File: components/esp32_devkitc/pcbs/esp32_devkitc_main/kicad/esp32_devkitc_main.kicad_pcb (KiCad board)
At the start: 2 copper layers, 65 x 56 mm, 10 parts, among them P1 Conn_02x20_Odd_Even

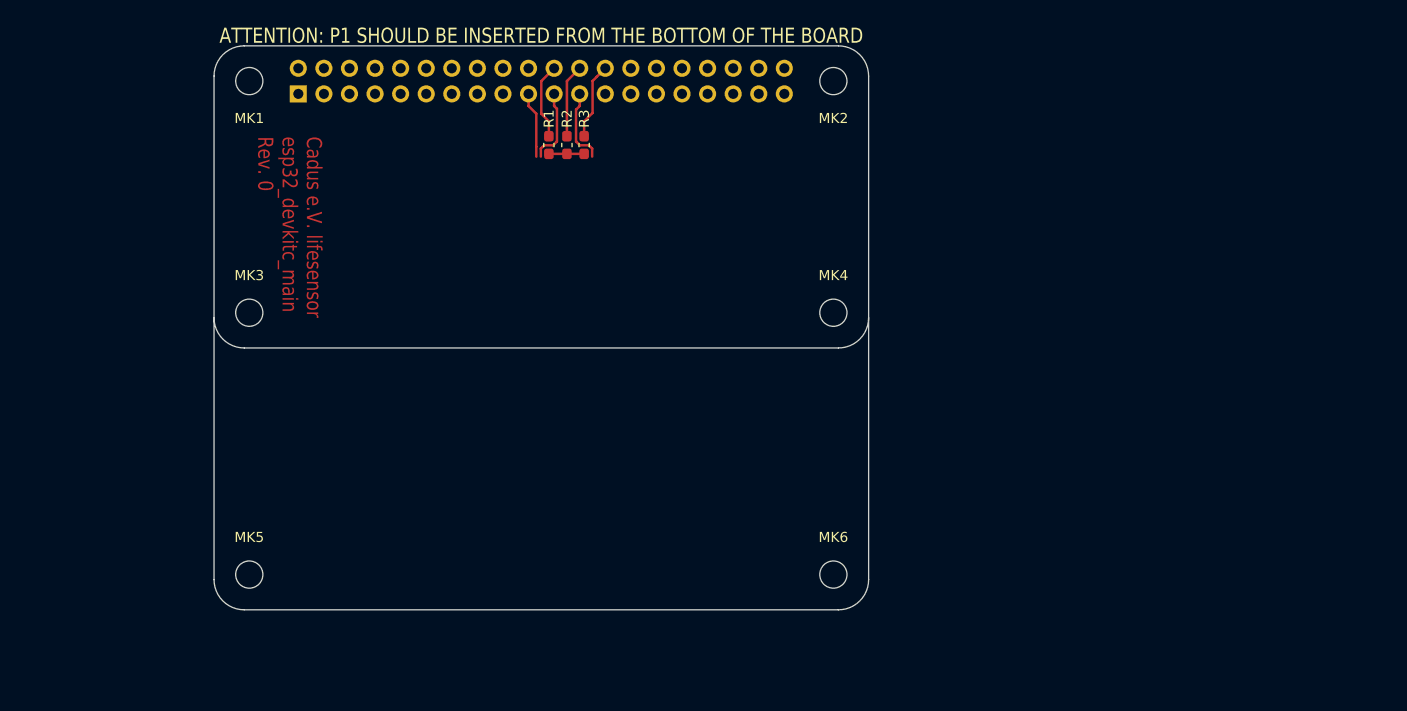
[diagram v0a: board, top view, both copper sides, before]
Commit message: add devkitc to board
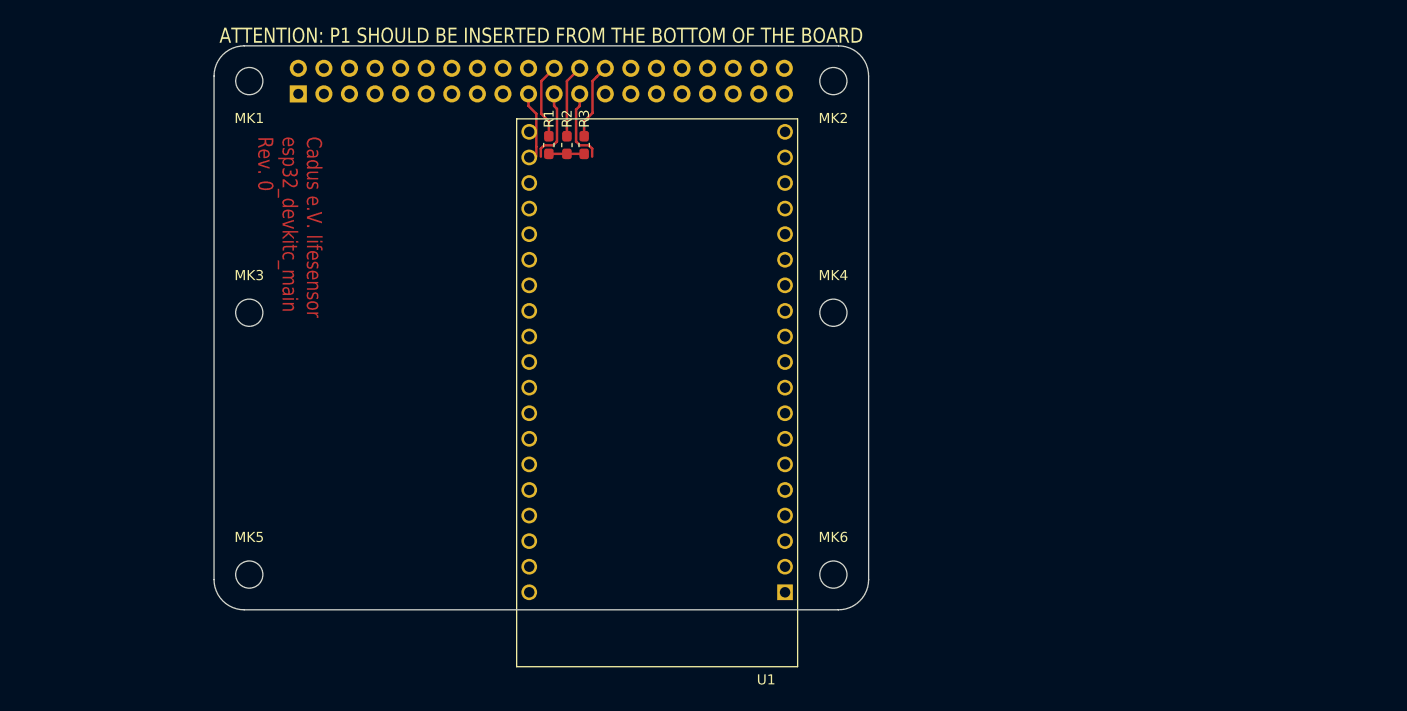
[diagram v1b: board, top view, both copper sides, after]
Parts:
- added U1: ESP32-DEVKITC-32D, lib_footprint:MODULE_ESP32-DEVKITC-32D, F.Cu at (244.0, 128.5)
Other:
- outline, holes or cut-outs redrawn
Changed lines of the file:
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@@
   (general
     (thickness 1.6)
-    (drawings 21)
+    (drawings 18)
     (tracks 32)
     (zones 0)
-    (modules 10)
-    (nets 35)
+    (modules 11)
+    (nets 73)
   )
   (page A3)
@@
   (net 33 /~SENS_CS_SPO2)
   (net 34 /~CS)
+  (net 35 "Net-(U1-Pad38)")
+  (net 36 "Net-(U1-Pad37)")
+  (net 37 "Net-(U1-Pad36)")
+  (net 38 "Net-(U1-Pad35)")
+  (net 39 "Net-(U1-Pad34)")
+  (net 40 "Net-(U1-Pad33)")
+  (net 41 "Net-(U1-Pad32)")
+  (net 42 "Net-(U1-Pad31)")
+  (net 43 "Net-(U1-Pad30)")
+  (net 44 "Net-(U1-Pad29)")
+  (net 45 "Net-(U1-Pad28)")
+  (net 46 "Net-(U1-Pad27)")
+  (net 47 "Net-(U1-Pad26)")
+  (net 48 "Net-(U1-Pad25)")
+  (net 49 "Net-(U1-Pad24)")
+  (net 50 "Net-(U1-Pad23)")
+  (net 51 "Net-(U1-Pad22)")
+  (net 52 "Net-(U1-Pad21)")
+  (net 53 "Net-(U1-Pad20)")
+  (net 54 "Net-(U1-Pad18)")
+  (net 55 "Net-(U1-Pad17)")
+  (net 56 "Net-(U1-Pad16)")
+  (net 57 "Net-(U1-Pad15)")
+  (net 58 "Net-(U1-Pad14)")
+  (net 59 "Net-(U1-Pad13)")
+  (net 60 "Net-(U1-Pad12)")
+  (net 61 "Net-(U1-Pad11)")
+  (net 62 "Net-(U1-Pad10)")
+  (net 63 "Net-(U1-Pad9)")
+  (net 64 "Net-(U1-Pad8)")
+  (net 65 "Net-(U1-Pad7)")
+  (net 66 "Net-(U1-Pad6)")
+  (net 67 "Net-(U1-Pad5)")
+  (net 68 "Net-(U1-Pad4)")
+  (net 69 "Net-(U1-Pad3)")
+  (net 70 "Net-(U1-Pad19)")
+  (net 71 "Net-(U1-Pad2)")
+  (net 72 "Net-(U1-Pad1)")
   (net_class Default "This is the default net class."
     (clearance 0.2)
@@
     (add_net /~SENS_RST_ECG)
     (add_net /~SENS_RST_SPO2)
+    (add_net "Net-(U1-Pad1)")
+    (add_net "Net-(U1-Pad10)")
+    (add_net "Net-(U1-Pad11)")
+    (add_net "Net-(U1-Pad12)")
+    (add_net "Net-(U1-Pad13)")
+    (add_net "Net-(U1-Pad14)")
+    (add_net "Net-(U1-Pad15)")
+    (add_net "Net-(U1-Pad16)")
+    (add_net "Net-(U1-Pad17)")
+    (add_net "Net-(U1-Pad18)")
+    (add_net "Net-(U1-Pad19)")
+    (add_net "Net-(U1-Pad2)")
+    (add_net "Net-(U1-Pad20)")
+    (add_net "Net-(U1-Pad21)")
+    (add_net "Net-(U1-Pad22)")
+    (add_net "Net-(U1-Pad23)")
+    (add_net "Net-(U1-Pad24)")
+    (add_net "Net-(U1-Pad25)")
+    (add_net "Net-(U1-Pad26)")
+    (add_net "Net-(U1-Pad27)")
+    (add_net "Net-(U1-Pad28)")
+    (add_net "Net-(U1-Pad29)")
+    (add_net "Net-(U1-Pad3)")
+    (add_net "Net-(U1-Pad30)")
+    (add_net "Net-(U1-Pad31)")
+    (add_net "Net-(U1-Pad32)")
+    (add_net "Net-(U1-Pad33)")
+    (add_net "Net-(U1-Pad34)")
+    (add_net "Net-(U1-Pad35)")
+    (add_net "Net-(U1-Pad36)")
+    (add_net "Net-(U1-Pad37)")
+    (add_net "Net-(U1-Pad38)")
+    (add_net "Net-(U1-Pad4)")
+    (add_net "Net-(U1-Pad5)")
+    (add_net "Net-(U1-Pad6)")
+    (add_net "Net-(U1-Pad7)")
+    (add_net "Net-(U1-Pad8)")
+    (add_net "Net-(U1-Pad9)")
   )
   (net_class Power ""
@@
     (add_net +5VD)
     (add_net GND)
+  )
+  (module lib_footprint:MODULE_ESP32-DEVKITC-32D (layer F.Cu)
+    (at 244 128.5 180)
+    (fp_text reference U1 (at -10.829175 -28.446045) (layer F.SilkS)
+      (effects (font (size 1.000386 1.000386) (thickness 0.015)))
+    )
+    (fp_text value ESP32-DEVKITC-32D (at 1.24136 28.294535) (layer F.Fab)
+      (effects (font (size 1.001047 1.001047) (thickness 0.015)))
+    )
+    (fp_circle (center -14.6 -19.9) (end -14.46 -19.9) (layer F.Fab) (width 0.28))
+    (fp_circle (center -14.6 -19.9) (end -14.46 -19.9) (layer F.Fab) (width 0.28))
+    (fp_line (start -14.2 27.5) (end -14.2 -27.4) (layer F.CrtYd) (width 0.05))
+    (fp_line (start 14.2 27.5) (end -14.2 27.5) (layer F.CrtYd) (width 0.05))
+    (fp_line (start 14.2 -27.4) (end 14.2 27.5) (layer F.CrtYd) (width 0.05))
+    (fp_line (start -14.2 -27.4) (end 14.2 -27.4) (layer F.CrtYd) (width 0.05))
+    (fp_line (start 13.95 27.25) (end -13.95 27.25) (layer F.SilkS) (width 0.127))
+    (fp_line (start 13.95 -27.15) (end 13.95 27.25) (layer F.SilkS) (width 0.127))
+    (fp_line (start -13.95 -27.15) (end 13.95 -27.15) (layer F.SilkS) (width 0.127))
+    (fp_line (start -13.95 27.25) (end -13.95 -27.15) (layer F.SilkS) (width 0.127))
+    (fp_line (start -13.95 27.25) (end -13.95 -27.15) (layer F.Fab) (width 0.127))
+    (fp_line (start 13.95 27.25) (end -13.95 27.25) (layer F.Fab) (width 0.127))
+    (fp_line (start 13.95 -27.15) (end 13.95 27.25) (layer F.Fab) (width 0.127))
+    (fp_line (start -13.95 -27.15) (end 13.95 -27.15) (layer F.Fab) (width 0.127))
+    (pad 38 thru_hole circle (at 12.7 25.96 180) (size 1.56 1.56) (drill 1.04) (layers *.Cu *.Mask)
+      (net 35 "Net-(U1-Pad38)"))
+    (pad 37 thru_hole circle (at 12.7 23.42 180) (size 1.56 1.56) (drill 1.04) (layers *.Cu *.Mask)
+      (net 36 "Net-(U1-Pad37)"))
+    (pad 36 thru_hole circle (at 12.7 20.88 180) (size 1.56 1.56) (drill 1.04) (layers *.Cu *.Mask)
+      (net 37 "Net-(U1-Pad36)"))
+    (pad 35 thru_hole circle (at 12.7 18.34 180) (size 1.56 1.56) (drill 1.04) (layers *.Cu *.Mask)
+      (net 38 "Net-(U1-Pad35)"))
+    (pad 34 thru_hole circle (at 12.7 15.8 180) (size 1.56 1.56) (drill 1.04) (layers *.Cu *.Mask)
+      (net 39 "Net-(U1-Pad34)"))
+    (pad 33 thru_hole circle (at 12.7 13.26 180) (size 1.56 1.56) (drill 1.04) (layers *.Cu *.Mask)
+      (net 40 "Net-(U1-Pad33)"))
+    (pad 32 thru_hole circle (at 12.7 10.72 180) (size 1.56 1.56) (drill 1.04) (layers *.Cu *.Mask)
+      (net 41 "Net-(U1-Pad32)"))
+    (pad 31 thru_hole circle (at 12.7 8.18 180) (size 1.56 1.56) (drill 1.04) (layers *.Cu *.Mask)
+      (net 42 "Net-(U1-Pad31)"))
+    (pad 30 thru_hole circle (at 12.7 5.64 180) (size 1.56 1.56) (drill 1.04) (layers *.Cu *.Mask)
+      (net 43 "Net-(U1-Pad30)"))
+    (pad 29 thru_hole circle (at 12.7 3.1 180) (size 1.56 1.56) (drill 1.04) (layers *.Cu *.Mask)
+      (net 44 "Net-(U1-Pad29)"))
+    (pad 28 thru_hole circle (at 12.7 0.56 180) (size 1.56 1.56) (drill 1.04) (layers *.Cu *.Mask)
+      (net 45 "Net-(U1-Pad28)"))
+    (pad 27 thru_hole circle (at 12.7 -1.98 180) (size 1.56 1.56) (drill 1.04) (layers *.Cu *.Mask)
+      (net 46 "Net-(U1-Pad27)"))
+    (pad 26 thru_hole circle (at 12.7 -4.52 180) (size 1.56 1.56) (drill 1.04) (layers *.Cu *.Mask)
+      (net 47 "Net-(U1-Pad26)"))
+    (pad 25 thru_hole circle (at 12.7 -7.06 180) (size 1.56 1.56) (drill 1.04) (layers *.Cu *.Mask)
+      (net 48 "Net-(U1-Pad25)"))
+    (pad 24 thru_hole circle (at 12.7 -9.6 180) (size 1.56 1.56) (drill 1.04) (layers *.Cu *.Mask)
+      (net 49 "Net-(U1-Pad24)"))
+    (pad 23 thru_hole circle (at 12.7 -12.14 180) (size 1.56 1.56) (drill 1.04) (layers *.Cu *.Mask)
+      (net 50 "Net-(U1-Pad23)"))
+    (pad 22 thru_hole circle (at 12.7 -14.68 180) (size 1.56 1.56) (drill 1.04) (layers *.Cu *.Mask)
+      (net 51 "Net-(U1-Pad22)"))
+    (pad 21 thru_hole circle (at 12.7 -17.22 180) (size 1.56 1.56) (drill 1.04) (layers *.Cu *.Mask)
+      (net 52 "Net-(U1-Pad21)"))
+    (pad 20 thru_hole circle (at 12.7 -19.76 180) (size 1.56 1.56) (drill 1.04) (layers *.Cu *.Mask)
+      (net 53 "Net-(U1-Pad20)"))
+    (pad 18 thru_hole circle (at -12.7 23.42 180) (size 1.56 1.56) (drill 1.04) (layers *.Cu *.Mask)
+      (net 54 "Net-(U1-Pad18)"))
+    (pad 17 thru_hole circle (at -12.7 20.88 180) (size 1.56 1.56) (drill 1.04) (layers *.Cu *.Mask)
+      (net 55 "Net-(U1-Pad17)"))
+    (pad 16 thru_hole circle (at -12.7 18.34 180) (size 1.56 1.56) (drill 1.04) (layers *.Cu *.Mask)
+      (net 56 "Net-(U1-Pad16)"))
+    (pad 15 thru_hole circle (at -12.7 15.8 180) (size 1.56 1.56) (drill 1.04) (layers *.Cu *.Mask)
+      (net 57 "Net-(U1-Pad15)"))
+    (pad 14 thru_hole circle (at -12.7 13.26 180) (size 1.56 1.56) (drill 1.04) (layers *.Cu *.Mask)
+      (net 58 "Net-(U1-Pad14)"))
+    (pad 13 thru_hole circle (at -12.7 10.72 180) (size 1.56 1.56) (drill 1.04) (layers *.Cu *.Mask)
+      (net 59 "Net-(U1-Pad13)"))
+    (pad 12 thru_hole circle (at -12.7 8.18 180) (size 1.56 1.56) (drill 1.04) (layers *.Cu *.Mask)
+      (net 60 "Net-(U1-Pad12)"))
+    (pad 11 thru_hole circle (at -12.7 5.64 180) (size 1.56 1.56) (drill 1.04) (layers *.Cu *.Mask)
+      (net 61 "Net-(U1-Pad11)"))
+    (pad 10 thru_hole circle (at -12.7 3.1 180) (size 1.56 1.56) (drill 1.04) (layers *.Cu *.Mask)
+      (net 62 "Net-(U1-Pad10)"))
+    (pad 9 thru_hole circle (at -12.7 0.56 180) (size 1.56 1.56) (drill 1.04) (layers *.Cu *.Mask)
+      (net 63 "Net-(U1-Pad9)"))
+    (pad 8 thru_hole circle (at -12.7 -1.98 180) (size 1.56 1.56) (drill 1.04) (layers *.Cu *.Mask)
+      (net 64 "Net-(U1-Pad8)"))
+    (pad 7 thru_hole circle (at -12.7 -4.52 180) (size 1.56 1.56) (drill 1.04) (layers *.Cu *.Mask)
+      (net 65 "Net-(U1-Pad7)"))
+    (pad 6 thru_hole circle (at -12.7 -7.06 180) (size 1.56 1.56) (drill 1.04) (layers *.Cu *.Mask)
+      (net 66 "Net-(U1-Pad6)"))
+    (pad 5 thru_hole circle (at -12.7 -9.6 180) (size 1.56 1.56) (drill 1.04) (layers *.Cu *.Mask)
+      (net 67 "Net-(U1-Pad5)"))
+    (pad 4 thru_hole circle (at -12.7 -12.14 180) (size 1.56 1.56) (drill 1.04) (layers *.Cu *.Mask)
+      (net 68 "Net-(U1-Pad4)"))
+    (pad 3 thru_hole circle (at -12.7 -14.68 180) (size 1.56 1.56) (drill 1.04) (layers *.Cu *.Mask)
+      (net 69 "Net-(U1-Pad3)"))
+    (pad 19 thru_hole circle (at -12.7 25.96 180) (size 1.56 1.56) (drill 1.04) (layers *.Cu *.Mask)
+      (net 70 "Net-(U1-Pad19)"))
+    (pad 2 thru_hole circle (at -12.7 -17.22 180) (size 1.56 1.56) (drill 1.04) (layers *.Cu *.Mask)
+      (net 71 "Net-(U1-Pad2)"))
+    (pad 1 thru_hole rect (at -12.7 -19.76 180) (size 1.56 1.56) (drill 1.04) (layers *.Cu *.Mask)
+      (net 72 "Net-(U1-Pad1)"))
   )
   (module Resistor_SMD:R_0603_1608Metric_Pad1.05x0.95mm_HandSolder (layer F.Cu)
@@
     (effects (font (size 2 1.7) (thickness 0.12)) (justify left))
   )
-  (gr_arc (start 203 121) (end 200 121) (angle -90) (layer Edge.Cuts) (width 0.1))
-  (gr_arc (start 262 121) (end 262 124) (angle -90) (layer Edge.Cuts) (width 0.1))
-  (gr_line (start 203 124) (end 262 124) (layer Edge.Cuts) (width 0.1))
   (gr_arc (start 262 97) (end 262 94) (angle 90) (layer Edge.Cuts) (width 0.1))
   (gr_arc (start 262 147) (end 265 147) (angle 90) (layer Edge.Cuts) (width 0.1))

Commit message: [WIP] develop ESP32-main pcb
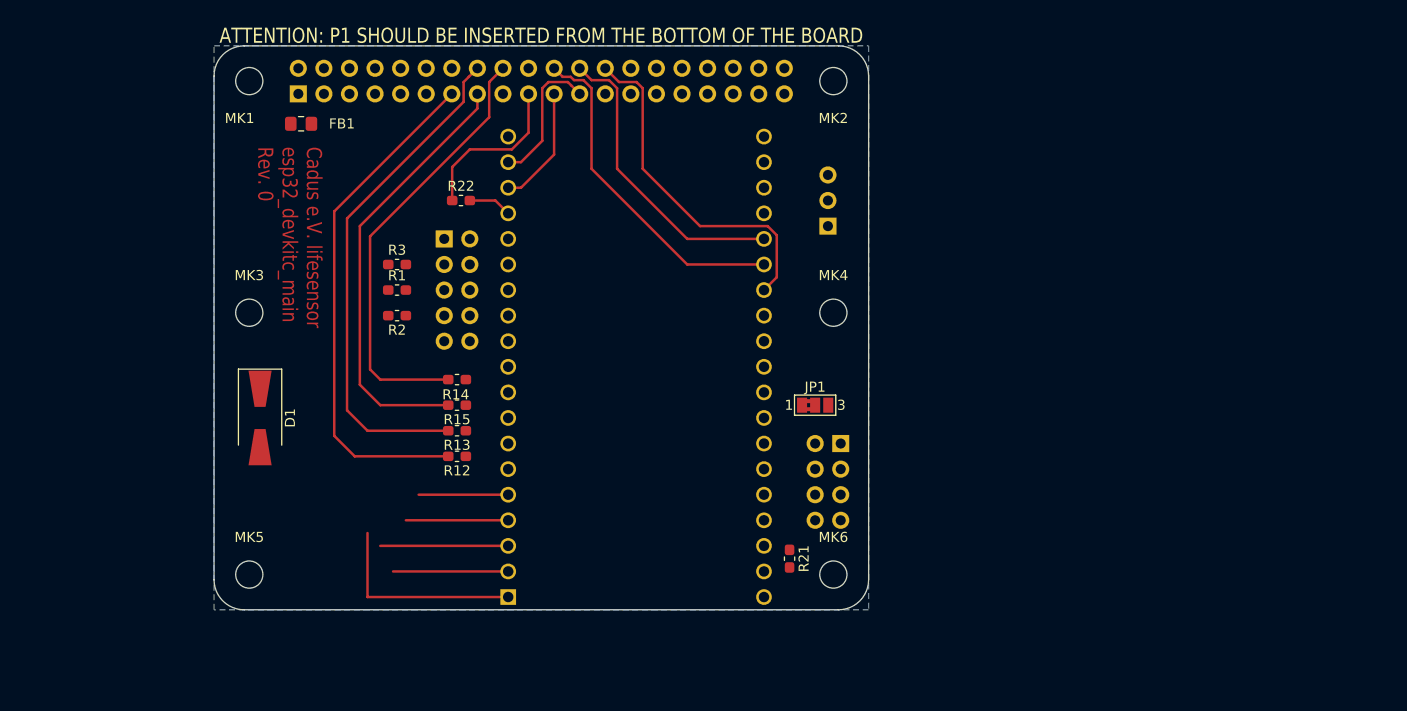
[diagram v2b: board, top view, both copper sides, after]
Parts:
- added D1: D, Diode_SMD:D_SMA-SMB_Universal_Handsoldering, F.Cu at (204.6, 130.9)
- added FB1: Ferrite_Bead_Small, Resistor_SMD:R_0805_2012Metric_Pad1.15x1.40mm_HandSolder, F.Cu at (208.6, 101.7)
- added J1: Conn_02x05_Odd_Even, Connector_PinSocket_2.54mm:PinSocket_2x05_P2.54mm_Vertical, B.Cu at (222.9, 113.2)
- added J2: Conn_02x04_Odd_Even, Connector_PinHeader_2.54mm:PinHeader_2x04_P2.54mm_Vertical, B.Cu at (262.2, 133.5)
- added J3: Conn_01x03_Male, Connector_PinHeader_2.54mm:PinHeader_1x03_P2.54mm_Vertical, B.Cu at (261.0, 111.9)
- added JP1: Jumper_NC_Dual, Jumper:SolderJumper-3_P1.3mm_Bridged2Bar12_Pad1.0x1.5mm_NumberLabels, F.Cu at (259.7, 129.7)
- added R12: 0, Resistor_SMD:R_0603_1608Metric_Pad1.05x0.95mm_HandSolder, F.Cu at (224.1, 134.8)
- added R13: 0, Resistor_SMD:R_0603_1608Metric_Pad1.05x0.95mm_HandSolder, F.Cu at (224.1, 132.2)
- added R14: 0, Resistor_SMD:R_0603_1608Metric_Pad1.05x0.95mm_HandSolder, F.Cu at (224.1, 127.1)
- added R15: 0, Resistor_SMD:R_0603_1608Metric_Pad1.05x0.95mm_HandSolder, F.Cu at (224.1, 129.7)
- added R21: 100, Resistor_SMD:R_0603_1608Metric_Pad1.05x0.95mm_HandSolder, F.Cu at (257.1, 144.9)
- added R22: 100, Resistor_SMD:R_0603_1608Metric_Pad1.05x0.95mm_HandSolder, F.Cu at (224.5, 109.4)
- R1, R3: value n.p. -> 0
- U1: moved to B.Cu
- moved R2 23.9 mm to (218.2, 120.8), turned to 180 degrees
- moved R3 22.0 mm to (218.2, 115.7), turned to 0 degrees
- moved R1 20.8 mm to (218.2, 118.2), turned to 0 degrees
- moved U1 2.14 mm to (241.9, 129.0), turned to 0 degrees
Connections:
- P1 pad 1: +3.3VA -> /SENS_3V3_ANA
- P1 pad 17: +3V3 -> /SENS_3V3_DIG
- P1 pad 2: +5VA -> /SENS_5V_ANA
- P1 pad 4: +5VD -> /SENS_5V_ANA
- R1 pad 1: /~CS -> /JTAG_~TRST
- R1 pad 2: /~SENS_CS_BPM -> Net-(J1-Pad5)
- R2 pad 1: /~CS -> /JTAG_~SRST
- R2 pad 2: /~SENS_CS_ECG -> GND
- R3 pad 1: /~CS -> GND
- R3 pad 2: /~SENS_CS_SPO2 -> /JTAG_RTCK
- U1 pad 1: Net-(U1-Pad1) -> /SENS_3V3_DIG
- U1 pad 12: Net-(U1-Pad12) -> /JTAG_TMS
- U1 pad 13: Net-(U1-Pad13) -> /JTAG_TDI
- U1 pad 14: Net-(U1-Pad14) -> GND
- U1 pad 15: Net-(U1-Pad15) -> /JTAG_TDO
- U1 pad 17: Net-(U1-Pad17) -> /SENS_MISO
- U1 pad 18: Net-(U1-Pad18) -> /SENS_SCLK
- U1 pad 19: Net-(U1-Pad19) -> /SENS_5V_ANA
- U1 pad 2: Net-(U1-Pad2) -> /JTAG_~TRST
- U1 pad 20: Net-(U1-Pad20) -> GND
- U1 pad 24: Net-(U1-Pad24) -> /DISP_CS_TOUCH
- U1 pad 25: Net-(U1-Pad25) -> /DISP_INT_TOUCH
- U1 pad 26: Net-(U1-Pad26) -> GND
- U1 pad 27: Net-(U1-Pad27) -> /DISP_MISO
- U1 pad 28: Net-(U1-Pad28) -> /DISP_SCLK
- U1 pad 29: Net-(U1-Pad29) -> /DISP_CS_DISP
- U1 pad 3: Net-(U1-Pad3) -> /SENS_INT_BPM
- U1 pad 32: Net-(U1-Pad32) -> /~SENS_CS_SPO2
- U1 pad 33: Net-(U1-Pad33) -> /~SENS_CS_BPM
- U1 pad 34: Net-(U1-Pad34) -> /~SENS_CS_ECG
- U1 pad 35: Net-(U1-Pad35) -> /PROC_SDA
- U1 pad 36: Net-(U1-Pad36) -> /PROC_SCL
- U1 pad 4: Net-(U1-Pad4) -> /SENS_INT_SPO2
- U1 pad 5: Net-(U1-Pad5) -> /SENS_INT_ECG
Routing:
- net /SENS_START: track 0.00 -> 51.0 mm
- net /~SENS_RST_ECG: track 0.00 -> 50.2 mm
- net /~SENS_RST_SPO2: track 0.00 -> 43.5 mm
- net /~SENS_RST_BPM: track 0.00 -> 43.3 mm
- net /~SENS_CS_SPO2: track 7.61 -> 34.6 mm
- net /~SENS_CS_BPM: track 7.58 -> 33.6 mm
- net /~SENS_CS_ECG: track 7.27 -> 30.0 mm
- net /SENS_3V3_DIG: track 0.00 -> 20.3 mm
- net /SENS_INT_BPM: track 0.00 -> 12.7 mm
- net /JTAG_~TRST: track 0.00 -> 11.4 mm
- net /SENS_INT_SPO2: track 0.00 -> 10.2 mm
- net /SENS_MOSI: track 6.55 -> 16.2 mm
- net /SENS_INT_ECG: track 0.00 -> 8.89 mm
- net /SENS_SCLK: track 7.56 -> 13.9 mm
- net /SENS_MISO: track 7.53 -> 12.0 mm
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- added copper zone on B.Cu, net GND

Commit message: sackgasse1
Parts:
- moved R1 35.4 mm to (252.7, 110.6), turned to 90 degrees
- moved R3 33.2 mm to (250.2, 106.8), turned to 270 degrees
- moved R22 25.7 mm to (250.2, 110.6), turned to 270 degrees
- moved J1 24.7 mm to (247.0, 108.1), turned to 90 degrees
- moved D1 24.1 mm to (203.8, 106.8)
- moved R12 22.9 mm to (224.1, 111.9), turned to 90 degrees
- moved R13 20.5 mm to (226.7, 111.9), turned to 90 degrees
- moved R2 20.0 mm to (233.7, 108.1), turned to 270 degrees
- moved R15 18.5 mm to (229.2, 111.9), turned to 90 degrees
- moved R14 17.0 mm to (231.8, 111.9), turned to 90 degrees
- moved U1 14.0 mm to (227.9, 128.4), turned to 270 degrees
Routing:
- net /DISP_CS_TOUCH: track 0.00 -> 49.4 mm
- net Net-(R21-Pad2): track 0.00 -> 48.4 mm
- net /SENS_START: track 51.0 -> 12.5 mm
- net /~SENS_CS_SPO2: track 34.6 -> 0.00 mm
- net /~SENS_RST_ECG: track 50.2 -> 16.0 mm
- net /~SENS_CS_BPM: track 33.6 -> 0.00 mm
- net /DISP_SCLK: track 0.00 -> 33.3 mm
- net /~SENS_CS_ECG: track 30.0 -> 0.00 mm
- net /~SENS_RST_BPM: track 43.3 -> 13.5 mm
- net /~SENS_RST_SPO2: track 43.5 -> 17.2 mm
- net /SENS_MISO: track 12.0 -> 31.5 mm
- net /SENS_SCLK: track 13.9 -> 28.7 mm
- net /SENS_5V_ANA: track 0.00 -> 12.1 mm
- net /SENS_INT_SPO2: track 10.2 -> 21.7 mm
- net /JTAG_~TRST: track 11.4 -> 0.00 mm
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
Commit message: updates temp
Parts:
- moved R1 40.7 mm to (212.1, 112.5), turned to 0 degrees
- moved J3 38.6 mm to (244.4, 146.8), turned to 270 degrees
- moved R21 34.3 mm to (222.9, 144.3), turned to 180 degrees
- moved J2 30.7 mm to (234.9, 147.5), turned to 90 degrees
- moved JP1 26.3 mm to (238.7, 145.6), turned to 90 degrees
- moved D1 5.85 mm to (209.5, 108.1), turned to 180 degrees
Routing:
- net /SENS_3V3_DIG: track 14.2 -> 110.9 mm
- net /~SENS_CS_SPO2: track 0.00 -> 70.2 mm
- net /~SENS_CS_BPM: track 0.00 -> 67.7 mm
- net /~SENS_CS_ECG: track 0.00 -> 65.8 mm
- net Net-(J1-Pad5): track 0.00 -> 40.3 mm
- net Net-(R21-Pad2): track 48.4 -> 12.6 mm
- net /SENS_5V_ANA: track 12.1 -> 43.6 mm
- net /DISP_SCLK: track 33.3 -> 5.46 mm
- net /DISP_CS_TOUCH: track 49.4 -> 21.9 mm
- net /DISP_INT_TOUCH: track 0.00 -> 10.0 mm
- net Net-(J2-Pad2): track 0.00 -> 9.15 mm
- net /DISP_CS_DISP: track 0.00 -> 7.96 mm
- net /DISP_MOSI: track 0.00 -> 7.35 mm
- net /PROC_SDA: track 0.00 -> 6.47 mm
- net /PROC_SCL: track 0.00 -> 6.01 mm
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- added copper zone on F.Cu, net GND
